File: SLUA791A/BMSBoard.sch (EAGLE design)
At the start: 11 parts, among them X1 22-23-2021

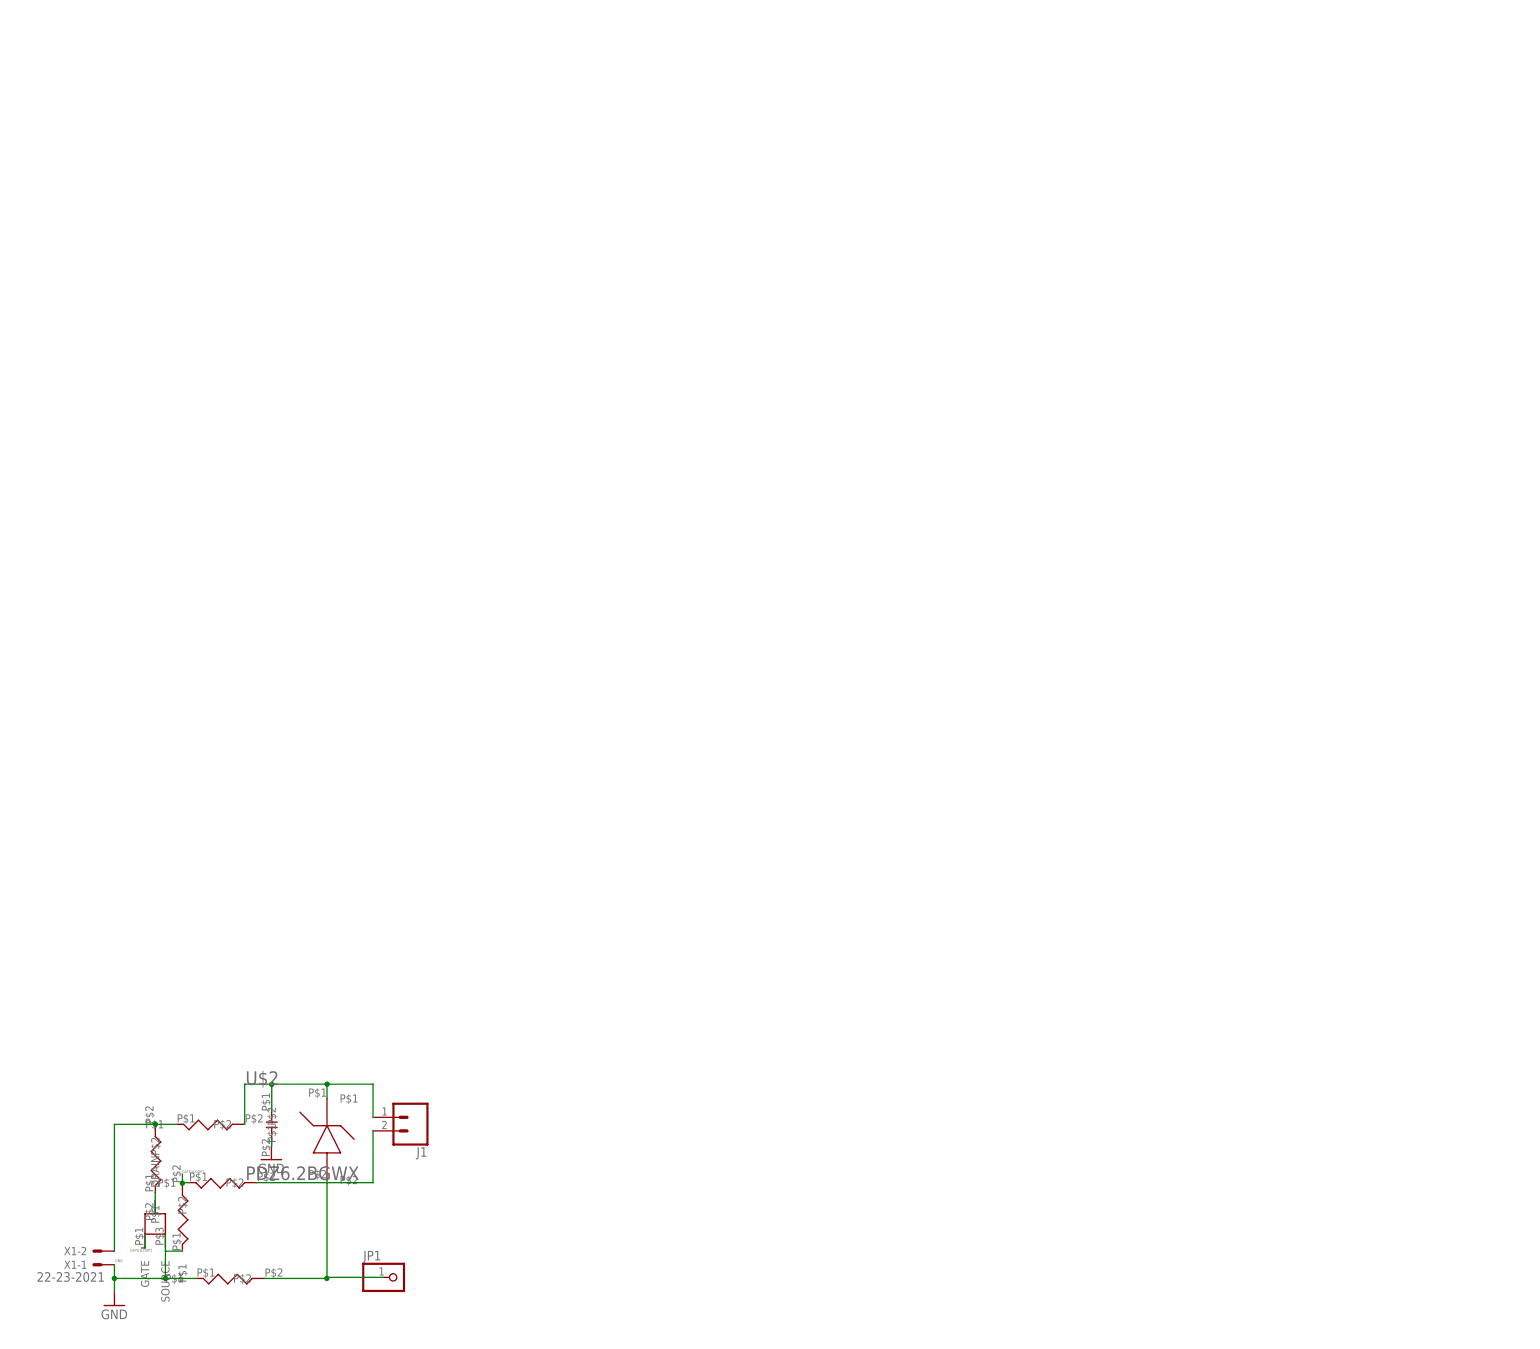
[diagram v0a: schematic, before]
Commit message: Added BMS Schematic
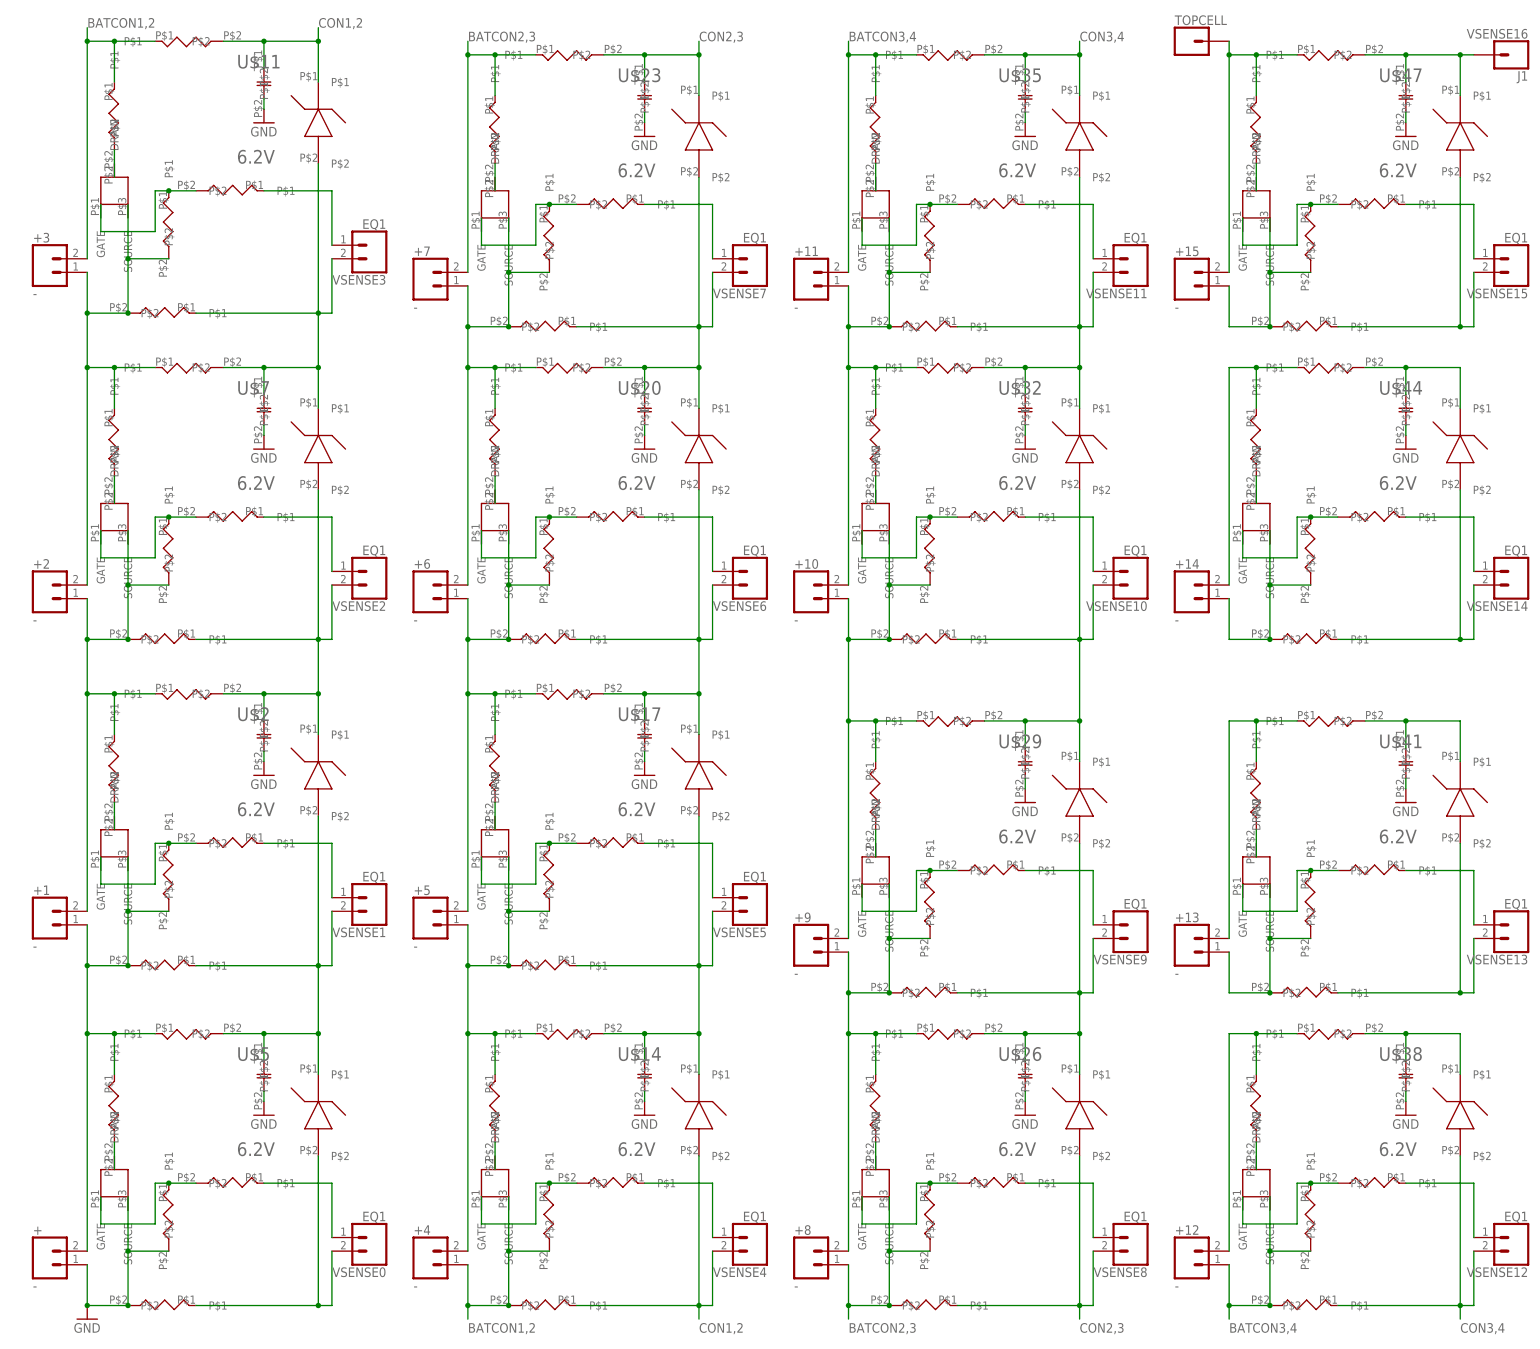
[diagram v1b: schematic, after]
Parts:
- removed JP1: (no value), adafruit:PINHD-1X1
- removed X1: 22-23-2021, con-molex:22-23-2021
- added +, +1, +10, +11, +12, +13, +14, +15, +2, +3, +4, +5, +6, +7, +8, +9: -, SparkFun-Connectors:CONN_02
- added 100KΩ, 100KΩ1, 100KΩ10, 100KΩ11, 100KΩ12, 100KΩ13, 100KΩ14, 100KΩ15, 100KΩ2, 100KΩ3, 100KΩ4, 100KΩ5, 100KΩ6, 100KΩ7, 100KΩ8, 100KΩ9: 100kΩ, Pod4:PWR3014W1000JE
- added 100Ω, 100Ω1, 100Ω10, 100Ω11, 100Ω12, 100Ω13, 100Ω14, 100Ω15, 100Ω2, 100Ω3, 100Ω4, 100Ω5, 100Ω6, 100Ω7, 100Ω8, 100Ω9, U$12, U$15, U$18, U$21, U$24, U$27, U$30, U$33, U$36, U$39, U$42, U$45, U$48, U$9: 100Ω, Pod4:PWR3014W1000JE
- added 1UF, 1UF1, 1UF10, 1UF11, 1UF12, 1UF13, 1UF14, 1UF15, 1UF2, 1UF3, 1UF4, 1UF5, 1UF6, 1UF7, 1UF8, 1UF9: 1uF, Pod4:CL21B105KBFNNNG
- added 2KΩ, 2KΩ1, 2KΩ10, 2KΩ11, 2KΩ12, 2KΩ13, 2KΩ14, 2KΩ15, 2KΩ2, 2KΩ3, 2KΩ4, 2KΩ5, 2KΩ6, 2KΩ7, 2KΩ8, 2KΩ9: 2kΩ, Pod4:PWR3014W1000JE
- added 75Ω, 75Ω1, 75Ω10, 75Ω11, 75Ω12, 75Ω13, 75Ω14, 75Ω15, 75Ω2, 75Ω3, 75Ω4, 75Ω5, 75Ω6, 75Ω7, 75Ω8, 75Ω9: 75Ω, Pod4:PWR3014W1000JE
- added TOPCELL: (no value), SparkFun-Connectors:CONN_01
- added U$10, U$13, U$16, U$19, U$22, U$25, U$28, U$31, U$34, U$37, U$40, U$43, U$46: 2V7002KT1G, Pod4:2V7002KT1G
- added U$11, U$14, U$17, U$20, U$23, U$26, U$29, U$32, U$35, U$38, U$41, U$44, U$47: 6.2V, Pod4:PDZ6.2BGWX
- added VSENSE0, VSENSE1, VSENSE10, VSENSE11, VSENSE12, VSENSE13, VSENSE14, VSENSE15, VSENSE2, VSENSE3, VSENSE4, VSENSE5, VSENSE6, VSENSE7, VSENSE8, VSENSE9: EQ1, SparkFun-Connectors:CONN_02
- J1: value (none) -> VSENSE16; device SparkFun-Connectors:CONN_02 -> SparkFun-Connectors:CONN_01
- U$2: value PDZ6.2BGWX -> 6.2V
- U$3: value PWR3014W1000JE -> 100Ω
- U$4, U$6: value PWR3014W1000JE -> 2V7002KT1G; device Pod4:PWR3014W1000JE -> Pod4:2V7002KT1G
- U$5, U$7: value PWR3014W1000JE -> 6.2V; device Pod4:PWR3014W1000JE -> Pod4:PDZ6.2BGWX
- U$8: value CL21B105KBFNNNG -> 100Ω; device Pod4:CL21B105KBFNNNG -> Pod4:PWR3014W1000JE
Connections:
- removed net GATE1LOOP1: U$1.GATE, U$3.P$2, U$4.P$1
- new net BATCON1,2: +3.2, +4.1, 100KΩ4.P$2, 100Ω4.P$2, 75Ω3.P$1, U$12.P$1, U$13.SOURCE
- new net BATCON2,3: +7.2, +8.1, 100KΩ8.P$2, 100Ω8.P$2, 75Ω7.P$1, U$24.P$1, U$25.SOURCE
- new net BATCON3,4: +11.2, +12.1, 100KΩ12.P$2, 100Ω12.P$2, 75Ω11.P$1, U$36.P$1, U$37.SOURCE
- new net CON1,2: 100Ω4.P$1, 1UF3.P$1, U$11.P$1, U$12.P$2, U$14.P$2, VSENSE4.2
- new net CON2,3: 100Ω8.P$1, 1UF7.P$1, U$23.P$1, U$24.P$2, U$26.P$2, VSENSE8.2
- new net CON3,4: 100Ω12.P$1, 1UF11.P$1, U$35.P$1, U$36.P$2, U$38.P$2, VSENSE12.2
- new net N$1: 100Ω.P$1, U$5.P$2, VSENSE0.2
- new net N$10: 75Ω1.P$2, U$1.DRAIN
- new net N$103: +10.2, +11.1, 100KΩ11.P$2, 100Ω11.P$2, 75Ω10.P$1, U$33.P$1, U$34.SOURCE
- new net N$105: +13.1, 100KΩ13.P$2, 100Ω13.P$2, U$40.SOURCE
- new net N$106: +14.1, 100KΩ14.P$2, 100Ω14.P$2, U$43.SOURCE
- new net N$107: +15.1, 100KΩ15.P$2, 100Ω15.P$2, U$46.SOURCE
- new net N$11: +1.2, +2.1, 100KΩ2.P$2, 100Ω2.P$2, 75Ω1.P$1, U$3.P$1, U$6.SOURCE
- new net N$13: 100Ω2.P$1, 1UF1.P$1, U$2.P$1, U$3.P$2, U$7.P$2, VSENSE2.2
- new net N$14: 100KΩ2.P$1, 2KΩ2.P$2, U$6.GATE
- new net N$15: 2KΩ2.P$1, VSENSE2.1
- new net N$16: 75Ω2.P$2, U$6.DRAIN
- new net N$19: 100Ω3.P$1, 1UF2.P$1, U$11.P$2, U$7.P$1, U$9.P$2, VSENSE3.2
- new net N$20: 100KΩ3.P$1, 2KΩ3.P$2, U$10.GATE
- new net N$21: 2KΩ3.P$1, VSENSE3.1
- new net N$22: 75Ω3.P$2, U$10.DRAIN
- new net N$26: 100KΩ4.P$1, 2KΩ4.P$2, U$13.GATE
- new net N$27: 2KΩ4.P$1, VSENSE4.1
- new net N$28: 75Ω4.P$2, U$13.DRAIN
- new net N$31: 100Ω5.P$1, 1UF4.P$1, U$14.P$1, U$15.P$2, U$17.P$2, VSENSE5.2
- new net N$32: 100KΩ5.P$1, 2KΩ5.P$2, U$16.GATE
- new net N$33: 2KΩ5.P$1, VSENSE5.1
- new net N$34: 75Ω5.P$2, U$16.DRAIN
- new net N$35: +5.2, +6.1, 100KΩ6.P$2, 100Ω6.P$2, 75Ω5.P$1, U$18.P$1, U$19.SOURCE
- new net N$36: 100Ω6.P$1, 1UF5.P$1, U$17.P$1, U$18.P$2, U$20.P$2, VSENSE6.2
- new net N$38: 100KΩ6.P$1, 2KΩ6.P$2, U$19.GATE
- new net N$39: 2KΩ6.P$1, VSENSE6.1
- new net N$4: 75Ω.P$2, U$4.DRAIN
- new net N$40: 75Ω6.P$2, U$19.DRAIN
- new net N$43: 100Ω7.P$1, 1UF6.P$1, U$20.P$1, U$21.P$2, U$23.P$2, VSENSE7.2
- new net N$44: 100KΩ7.P$1, 2KΩ7.P$2, U$22.GATE
- new net N$45: 2KΩ7.P$1, VSENSE7.1
- new net N$46: 75Ω7.P$2, U$22.DRAIN
- new net N$50: 100KΩ8.P$1, 2KΩ8.P$2, U$25.GATE
- new net N$51: 2KΩ8.P$1, VSENSE8.1
- new net N$52: 75Ω8.P$2, U$25.DRAIN
- new net N$53: +8.2, +9.1, 100KΩ9.P$2, 100Ω9.P$2, 75Ω8.P$1, U$27.P$1, U$28.SOURCE
- new net N$54: 100Ω9.P$1, 1UF8.P$1, U$26.P$1, U$27.P$2, U$29.P$2, VSENSE9.2
- new net N$56: 100KΩ9.P$1, 2KΩ9.P$2, U$28.GATE
- new net N$57: 2KΩ9.P$1, VSENSE9.1
- new net N$58: 75Ω9.P$2, U$28.DRAIN
- new net N$59: +10.1, +9.2, 100KΩ10.P$2, 100Ω10.P$2, 75Ω9.P$1, U$30.P$1, U$31.SOURCE
- new net N$60: 100Ω10.P$1, 1UF9.P$1, U$29.P$1, U$30.P$2, U$32.P$2, VSENSE10.2
- new net N$62: 100KΩ10.P$1, 2KΩ10.P$2, U$31.GATE
- new net N$63: 2KΩ10.P$1, VSENSE10.1
- new net N$64: 75Ω10.P$2, U$31.DRAIN
- new net N$66: 100Ω11.P$1, 1UF10.P$1, U$32.P$1, U$33.P$2, U$35.P$2, VSENSE11.2
- new net N$68: 100KΩ11.P$1, 2KΩ11.P$2, U$34.GATE
- new net N$69: 2KΩ11.P$1, VSENSE11.1
- new net N$70: 75Ω11.P$2, U$34.DRAIN
- new net N$74: 100KΩ12.P$1, 2KΩ12.P$2, U$37.GATE
- new net N$75: 2KΩ12.P$1, VSENSE12.1
- new net N$76: 75Ω12.P$2, U$37.DRAIN
- new net N$77: +12.2, 75Ω12.P$1, U$39.P$1
- new net N$78: 1UF12.P$1, U$38.P$1, U$39.P$2
- new net N$79: 100Ω13.P$1, U$41.P$2, VSENSE13.2
- new net N$80: 100KΩ13.P$1, 2KΩ13.P$2, U$40.GATE
- new net N$81: 2KΩ13.P$1, VSENSE13.1
- new net N$82: 75Ω13.P$2, U$40.DRAIN
- new net N$83: +13.2, 75Ω13.P$1, U$42.P$1
- new net N$84: 1UF13.P$1, U$41.P$1, U$42.P$2
- new net N$85: 100Ω14.P$1, U$44.P$2, VSENSE14.2
- new net N$86: 100KΩ14.P$1, 2KΩ14.P$2, U$43.GATE
- new net N$87: 2KΩ14.P$1, VSENSE14.1
- new net N$88: 75Ω14.P$2, U$43.DRAIN
- new net N$89: +14.2, 75Ω14.P$1, U$45.P$1
- new net N$9: 2KΩ1.P$1, VSENSE1.1
- new net N$90: 1UF14.P$1, U$44.P$1, U$45.P$2
- new net N$91: 100Ω15.P$1, U$47.P$2, VSENSE15.2
- new net N$92: 100KΩ15.P$1, 2KΩ15.P$2, U$46.GATE
- new net N$93: 2KΩ15.P$1, VSENSE15.1
- new net N$94: 75Ω15.P$2, U$46.DRAIN
- new net N$95: +15.2, 75Ω15.P$1, TOPCELL.1, U$48.P$1
- new net N$96: 1UF15.P$1, J1.1, U$47.P$1, U$48.P$2
- new net N$97: +4.2, +5.1, 100KΩ5.P$2, 100Ω5.P$2, 75Ω4.P$1, U$15.P$1, U$16.SOURCE
- new net N$99: +6.2, +7.1, 100KΩ7.P$2, 100Ω7.P$2, 75Ω6.P$1, U$21.P$1, U$22.SOURCE
- net GND: now also +.1, 100KΩ.P$2, 100Ω.P$2, 1UF.P$2, 1UF1.P$2, 1UF10.P$2, 1UF11.P$2, 1UF12.P$2, 1UF13.P$2, 1UF14.P$2, 1UF15.P$2, 1UF2.P$2, 1UF3.P$2, 1UF4.P$2, 1UF5.P$2, 1UF6.P$2, 1UF7.P$2, 1UF8.P$2, 1UF9.P$2, U$4.SOURCE; no longer U$1.SOURCE, U$3.P$1, U$5.P$1, U$8.P$2, X1-1.S
- net N$2: now also 100KΩ.P$1, 2KΩ.P$2, U$4.GATE; no longer JP1.1
- net N$3: now also 2KΩ.P$1, VSENSE0.1; no longer J1.2, U$4.P$2
- net N$5: now also +.2, +1.1, 100KΩ1.P$2, 100Ω1.P$2, 75Ω.P$1, U$1.SOURCE, U$8.P$1; no longer U$2.P$2, U$5.P$2
- net N$6: now also +2.2, +3.1, 100KΩ3.P$2, 100Ω3.P$2, 75Ω2.P$1, U$10.SOURCE, U$9.P$1; no longer U$1.DRAIN, U$6.P$1
- net N$7: now also 100Ω1.P$1, 1UF.P$1, U$2.P$2, U$5.P$1, U$8.P$2, VSENSE1.2; no longer J1.1, U$2.P$1, U$7.P$2, U$8.P$1
- net N$8: now also 100KΩ1.P$1, 2KΩ1.P$2, U$1.GATE; no longer U$6.P$2, U$7.P$1, X1-2.S
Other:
- moved on the sheet: U$2

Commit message: Updated BMSBoard
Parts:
- added GPIO_0-6: (no value), adafruit:PINHD-1X6
- added JP1: (no value), adafruit:PINHD-1X8BIG
- added U$49: BQ76PL455A-Q1, Pod4:BQ76PL455A-Q1
- added U$50: 22nF, Pod4:CL21B105KBFNNNG
- added U$51, U$52, U$54, U$55, U$56, U$57, U$58, U$59, U$60, U$61: CL21B105KBFNNNG, Pod4:CL21B105KBFNNNG
- added U$53: 1Ω, Pod4:PWR3014W1000JE
- added U$62, U$63: PWR3014W1000JE, Pod4:PWR3014W1000JE
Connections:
- removed net CON1,2: 100Ω4.P$1, 1UF3.P$1, U$11.P$1, U$12.P$2, U$14.P$2, VSENSE4.2
- removed net CON2,3: 100Ω8.P$1, 1UF7.P$1, U$23.P$1, U$24.P$2, U$26.P$2, VSENSE8.2
- removed net CON3,4: 100Ω12.P$1, 1UF11.P$1, U$35.P$1, U$36.P$2, U$38.P$2, VSENSE12.2
- removed net N$1: 100Ω.P$1, U$5.P$2, VSENSE0.2
- removed net N$13: 100Ω2.P$1, 1UF1.P$1, U$2.P$1, U$3.P$2, U$7.P$2, VSENSE2.2
- removed net N$15: 2KΩ2.P$1, VSENSE2.1
- removed net N$19: 100Ω3.P$1, 1UF2.P$1, U$11.P$2, U$7.P$1, U$9.P$2, VSENSE3.2
- removed net N$21: 2KΩ3.P$1, VSENSE3.1
- removed net N$27: 2KΩ4.P$1, VSENSE4.1
- removed net N$31: 100Ω5.P$1, 1UF4.P$1, U$14.P$1, U$15.P$2, U$17.P$2, VSENSE5.2
- removed net N$33: 2KΩ5.P$1, VSENSE5.1
- removed net N$36: 100Ω6.P$1, 1UF5.P$1, U$17.P$1, U$18.P$2, U$20.P$2, VSENSE6.2
- removed net N$39: 2KΩ6.P$1, VSENSE6.1
- removed net N$43: 100Ω7.P$1, 1UF6.P$1, U$20.P$1, U$21.P$2, U$23.P$2, VSENSE7.2
- removed net N$45: 2KΩ7.P$1, VSENSE7.1
- removed net N$51: 2KΩ8.P$1, VSENSE8.1
- removed net N$54: 100Ω9.P$1, 1UF8.P$1, U$26.P$1, U$27.P$2, U$29.P$2, VSENSE9.2
- removed net N$57: 2KΩ9.P$1, VSENSE9.1
- removed net N$60: 100Ω10.P$1, 1UF9.P$1, U$29.P$1, U$30.P$2, U$32.P$2, VSENSE10.2
- removed net N$63: 2KΩ10.P$1, VSENSE10.1
- removed net N$66: 100Ω11.P$1, 1UF10.P$1, U$32.P$1, U$33.P$2, U$35.P$2, VSENSE11.2
- removed net N$69: 2KΩ11.P$1, VSENSE11.1
- removed net N$7: 100Ω1.P$1, 1UF.P$1, U$2.P$2, U$5.P$1, U$8.P$2, VSENSE1.2
- removed net N$75: 2KΩ12.P$1, VSENSE12.1
- removed net N$78: 1UF12.P$1, U$38.P$1, U$39.P$2
- removed net N$79: 100Ω13.P$1, U$41.P$2, VSENSE13.2
- removed net N$81: 2KΩ13.P$1, VSENSE13.1
- removed net N$84: 1UF13.P$1, U$41.P$1, U$42.P$2
- removed net N$85: 100Ω14.P$1, U$44.P$2, VSENSE14.2
- removed net N$87: 2KΩ14.P$1, VSENSE14.1
- removed net N$9: 2KΩ1.P$1, VSENSE1.1
- removed net N$90: 1UF14.P$1, U$44.P$1, U$45.P$2
- removed net N$91: 100Ω15.P$1, U$47.P$2, VSENSE15.2
- removed net N$93: 2KΩ15.P$1, VSENSE15.1
- removed net N$96: 1UF15.P$1, J1.1, U$47.P$1, U$48.P$2
- new net AUX0: JP1.1, U$49.AUX0
- new net AUX1: JP1.2, U$49.AUX1
- new net AUX2: JP1.3, U$49.AUX2
- new net AUX3: JP1.4, U$49.AUX3
- new net AUX4: JP1.5, U$49.AUX4
- new net AUX5: JP1.6, U$49.AUX5
- new net AUX6: JP1.7, U$49.AUX6
- new net AUX7: JP1.8, U$49.AUX7
- new net COMMH+: U$49.COMMH+
- new net COMMH-: U$49.COMMH-
- new net COMML+: U$49.COMML+
- new net COMML-: U$49.COMML-
- new net EQ1: 2KΩ.P$1, U$49.EQ1, VSENSE0.1
- new net EQ10: 2KΩ9.P$1, U$49.EQ10, VSENSE9.1
- new net EQ11: 2KΩ10.P$1, U$49.EQ11, VSENSE10.1
- new net EQ12: 2KΩ11.P$1, U$49.EQ12, VSENSE11.1
- new net EQ13: 2KΩ12.P$1, U$49.EQ13, VSENSE12.1
- new net EQ14: 2KΩ13.P$1, U$49.EQ14, VSENSE13.1
- new net EQ15: 2KΩ14.P$1, U$49.EQ15, VSENSE14.1
- new net EQ16: 2KΩ15.P$1, U$49.EQ16, VSENSE15.1
- new net EQ2: 2KΩ1.P$1, U$49.EQ2, VSENSE1.1
- new net EQ3: 2KΩ2.P$1, U$49.EQ3, VSENSE2.1
- new net EQ4: 2KΩ3.P$1, U$49.EQ4, VSENSE3.1
- new net EQ5: 2KΩ4.P$1, U$49.EQ5, VSENSE4.1
- new net EQ6: 2KΩ5.P$1, U$49.EQ6, VSENSE5.1
- new net EQ7: 2KΩ6.P$1, U$49.EQ7, VSENSE6.1
- new net EQ8: 2KΩ7.P$1, U$49.EQ8, VSENSE7.1
- new net EQ9: 2KΩ8.P$1, U$49.EQ9, VSENSE8.1
- new net FAULTH+: U$49.FAULTH+
- new net FAULTH-: U$49.FAULTH-
- new net FAULTL+: U$49.FAULTL+
- new net FAULTL-: U$49.FAULTL-
- new net N$112: U$49.VM, U$51.P$1, U$52.P$1
- new net N$113: U$49.CHP, U$50.P$1
- new net N$114: U$49.CHM, U$50.P$2
- new net N$123: GPIO_0-6.6, U$49.GPIO5
- new net N$124: GPIO_0-6.5, U$49.GPIO4
- new net N$125: GPIO_0-6.4, U$49.GPIO3
- new net N$126: GPIO_0-6.3, U$49.GPIO2
- new net N$127: GPIO_0-6.2, U$49.GPIO1
- new net N$128: GPIO_0-6.1, U$49.GPIO0
- new net N$139: U$49.V5VAO, U$56.P$1
- new net N$151: U$49.VP, U$60.P$2, U$61.P$2
- new net N$152: U$49.NPNB
- new net OUT1: U$49.OUT1, U$49.OUT2, U$59.P$2
- new net TOP: U$49.TOP, U$63.P$2
- new net UART-INPUT: U$49.RX
- new net UART-OUTPUT: U$49.TX
- new net VDIG: U$49.VDIG, U$49.VIO, U$53.P$1, U$54.P$1, U$55.P$1
- new net VP: U$53.P$2
- new net VREF: U$49.VREF, U$57.P$2, U$58.P$2
- new net VSENSE0: 100Ω.P$1, U$49.VSENSE0, U$5.P$2, VSENSE0.2
- new net VSENSE1: 100Ω1.P$1, 1UF.P$1, U$2.P$2, U$49.VSENSE1, U$5.P$1, U$8.P$2, VSENSE1.2
- new net VSENSE10: 100Ω10.P$1, 1UF9.P$1, U$29.P$1, U$30.P$2, U$32.P$2, U$49.VSENSE10, VSENSE10.2
- new net VSENSE11: 100Ω11.P$1, 1UF10.P$1, U$32.P$1, U$33.P$2, U$35.P$2, U$49.VSENSE11, VSENSE11.2
- new net VSENSE12: 100Ω12.P$1, 1UF11.P$1, U$35.P$1, U$36.P$2, U$38.P$2, U$49.VSENSE12, VSENSE12.2
- new net VSENSE13: 100Ω13.P$1, 1UF12.P$1, U$38.P$1, U$39.P$2, U$41.P$2, U$49.VSENSE13, VSENSE13.2
- new net VSENSE14: 100Ω14.P$1, 1UF13.P$1, U$41.P$1, U$42.P$2, U$44.P$2, U$49.VSENSE14, VSENSE14.2
- new net VSENSE15: 100Ω15.P$1, 1UF14.P$1, U$44.P$1, U$45.P$2, U$47.P$2, U$49.VSENSE15, VSENSE15.2
- new net VSENSE16: 1UF15.P$1, J1.1, U$47.P$1, U$48.P$2, U$49.VSENSE16
- new net VSENSE2: 100Ω2.P$1, 1UF1.P$1, U$2.P$1, U$3.P$2, U$49.VSENSE2, U$7.P$2, VSENSE2.2
- new net VSENSE3: 100Ω3.P$1, 1UF2.P$1, U$11.P$2, U$49.VSENSE3, U$7.P$1, U$9.P$2, VSENSE3.2
- new net VSENSE4: 100Ω4.P$1, 1UF3.P$1, U$11.P$1, U$12.P$2, U$14.P$2, U$49.VSENSE4, VSENSE4.2
- new net VSENSE5: 100Ω5.P$1, 1UF4.P$1, U$14.P$1, U$15.P$2, U$17.P$2, U$49.VSENSE5, VSENSE5.2
- new net VSENSE6: 100Ω6.P$1, 1UF5.P$1, U$17.P$1, U$18.P$2, U$20.P$2, U$49.VSENSE6, VSENSE6.2
- new net VSENSE7: 100Ω7.P$1, 1UF6.P$1, U$20.P$1, U$21.P$2, U$23.P$2, U$49.VSENSE7, VSENSE7.2
- new net VSENSE8: 100Ω8.P$1, 1UF7.P$1, U$23.P$1, U$24.P$2, U$26.P$2, U$49.VSENSE8, VSENSE8.2
- new net VSENSE9: 100Ω9.P$1, 1UF8.P$1, U$26.P$1, U$27.P$2, U$29.P$2, U$49.VSENSE9, VSENSE9.2
- net GND: now also U$49.AGND1, U$49.AGND2, U$49.AGND3, U$49.CGND, U$49.DGND1, U$49.DG_ND2, U$49.DG_ND3, U$49.WAKEUP, U$51.P$2, U$52.P$2, U$54.P$2, U$55.P$2, U$56.P$2, U$57.P$1, U$58.P$1, U$59.P$1, U$60.P$1, U$62.P$2
- net N$3: now also U$61.P$1, U$62.P$1; no longer 2KΩ.P$1, VSENSE0.1
- net N$95: now also U$63.P$1
